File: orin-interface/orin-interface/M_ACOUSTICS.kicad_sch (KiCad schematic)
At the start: 19 parts, among them T6 749022310

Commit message: orin-interface: PoE channels, buses, 3V3 regulator, ERC fixes
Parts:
- C52, C53, C54, C55, C56, C57, C58, C59, C60, C61: footprint (none) -> Capacitor_SMD:C_0603_1608Metric_Pad1.08x0.95mm_HandSolder
- R32, R36, R40, R44, R57, R58, R59, R60: footprint (none) -> Resistor_SMD:R_0603_1608Metric_Pad0.98x0.95mm_HandSolder
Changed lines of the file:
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@@
 			)
 		)
-		(property "Footprint" ""
+		(property "Footprint" "Resistor_SMD:R_0603_1608Metric_Pad0.98x0.95mm_HandSolder"
 			(at 119.38 74.93 0)
 			(hide yes)
@@
 			)
 		)
-		(property "Footprint" ""
+		(property "Footprint" "Capacitor_SMD:C_0603_1608Metric_Pad1.08x0.95mm_HandSolder"
 			(at 83.82 81.28 0)
 			(hide yes)
@@
 			)
 		)
-		(property "Footprint" ""
+		(property "Footprint" "Capacitor_SMD:C_0603_1608Metric_Pad1.08x0.95mm_HandSolder"
 			(at 86.36 88.9 0)
 			(hide yes)
@@
 			)
 		)
-		(property "Footprint" ""
+		(property "Footprint" "Resistor_SMD:R_0603_1608Metric_Pad0.98x0.95mm_HandSolder"
 			(at 88.9 74.93 0)
 			(hide yes)
@@
 			)
 		)
-		(property "Footprint" ""
+		(property "Footprint" "Resistor_SMD:R_0603_1608Metric_Pad0.98x0.95mm_HandSolder"
 			(at 124.46 74.93 0)
 			(hide yes)
@@
 			)
 		)
-		(property "Footprint" ""
+		(property "Footprint" "Resistor_SMD:R_0603_1608Metric_Pad0.98x0.95mm_HandSolder"
 			(at 93.98 74.93 0)
 			(hide yes)
@@
 			)
 		)
-		(property "Footprint" ""
+		(property "Footprint" "Capacitor_SMD:C_0603_1608Metric_Pad1.08x0.95mm_HandSolder"
 			(at 119.38 81.28 0)
 			(hide yes)
@@
 			)
 		)
-		(property "Footprint" ""
+		(property "Footprint" "Resistor_SMD:R_0603_1608Metric_Pad0.98x0.95mm_HandSolder"
 			(at 78.74 74.93 0)
 			(hide yes)
@@
 			)
 		)
-		(property "Footprint" ""
+		(property "Footprint" "Capacitor_SMD:C_0603_1608Metric_Pad1.08x0.95mm_HandSolder"
 			(at 78.74 81.28 0)
 			(hide yes)
@@
 			)
 		)
-		(property "Footprint" ""
+		(property "Footprint" "Resistor_SMD:R_0603_1608Metric_Pad0.98x0.95mm_HandSolder"
 			(at 129.54 74.93 0)
 			(hide yes)
@@
 			)
 		)
-		(property "Footprint" ""
+		(property "Footprint" "Capacitor_SMD:C_0603_1608Metric_Pad1.08x0.95mm_HandSolder"
 			(at 88.9 81.28 0)
 			(hide yes)
@@
 			)
 		)
-		(property "Footprint" ""
+		(property "Footprint" "Capacitor_SMD:C_0603_1608Metric_Pad1.08x0.95mm_HandSolder"
 			(at 93.98 81.28 0)
 			(hide yes)
@@
 			)
 		)
-		(property "Footprint" ""
+		(property "Footprint" "Capacitor_SMD:C_0603_1608Metric_Pad1.08x0.95mm_HandSolder"
 			(at 129.54 81.28 0)
 			(hide yes)
@@
 			)
 		)
-		(property "Footprint" ""
+		(property "Footprint" "Capacitor_SMD:C_0603_1608Metric_Pad1.08x0.95mm_HandSolder"
 			(at 124.46 81.28 0)
 			(hide yes)
@@
 			)
 		)
-		(property "Footprint" ""
+		(property "Footprint" "Resistor_SMD:R_0603_1608Metric_Pad0.98x0.95mm_HandSolder"
 			(at 134.62 74.93 0)
 			(hide yes)
@@
 			)
 		)
-		(property "Footprint" ""
+		(property "Footprint" "Capacitor_SMD:C_0603_1608Metric_Pad1.08x0.95mm_HandSolder"
 			(at 127 88.9 0)
 			(hide yes)
@@
 			)
 		)
-		(property "Footprint" ""
+		(property "Footprint" "Resistor_SMD:R_0603_1608Metric_Pad0.98x0.95mm_HandSolder"
 			(at 83.82 74.93 0)
 			(hide yes)
@@
 			)
 		)
-		(property "Footprint" ""
+		(property "Footprint" "Capacitor_SMD:C_0603_1608Metric_Pad1.08x0.95mm_HandSolder"
 			(at 134.62 81.28 0)
 			(hide yes)

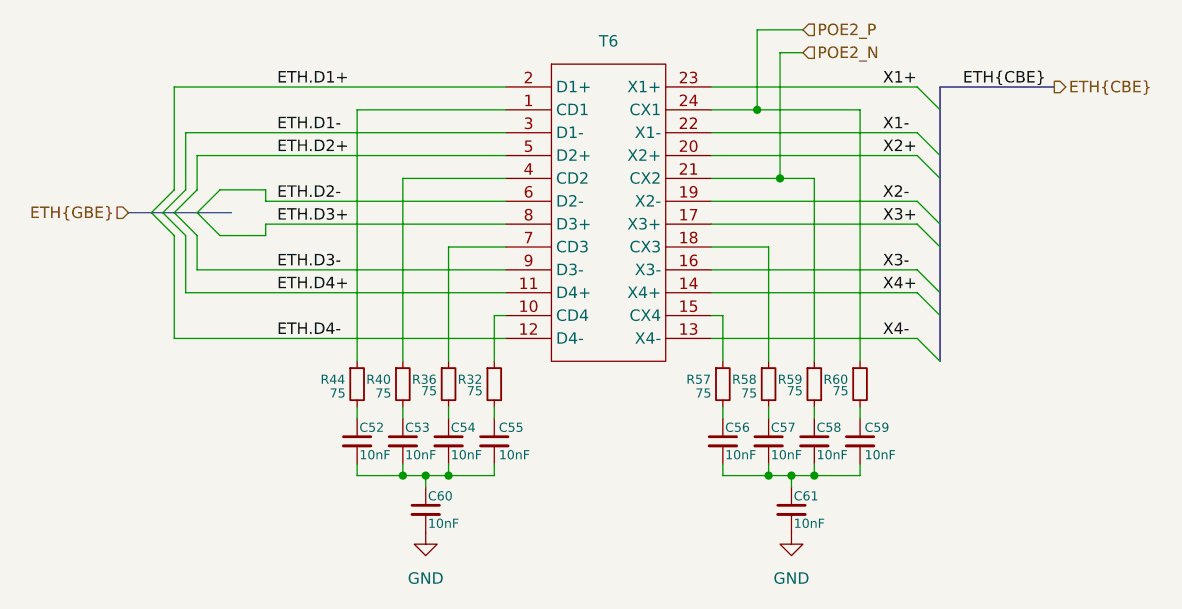
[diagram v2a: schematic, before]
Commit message: orin-interface: add ETH connector sheets and Mate-connectors footprint lib; update orin-bob
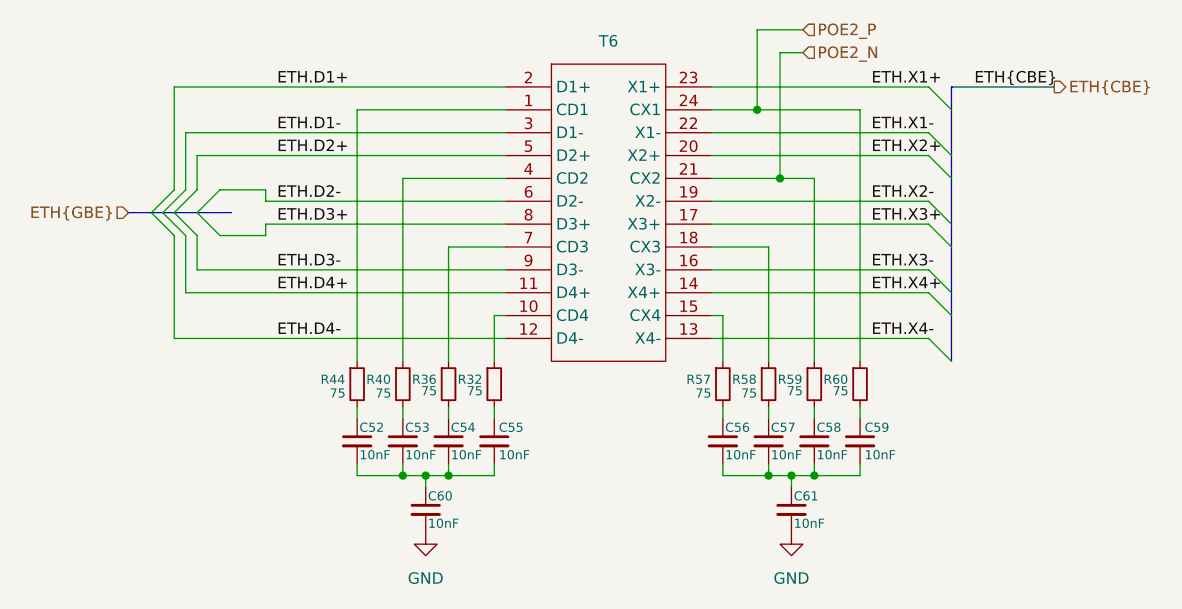
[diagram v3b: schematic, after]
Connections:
- net X1+ renamed ETH.X1+
- net X1- renamed ETH.X1-
- net X2+ renamed ETH.X2+
- net X2- renamed ETH.X2-
- net X3+ renamed ETH.X3+
- net X3- renamed ETH.X3-
- net X4+ renamed ETH.X4+
- net X4- renamed ETH.X4-
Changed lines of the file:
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@@
 	)
 	(bus_entry
-		(at 140.97 69.85)
+		(at 142.24 69.85)
 		(size 2.54 2.54)
 		(stroke
@@
 	)
 	(bus_entry
-		(at 140.97 41.91)
-		(size 2.54 2.54)
-		(stroke
-			(width 0)
-			(type default)
-		)
-	)
-	(bus_entry
-		(at 140.97 62.23)
+		(at 142.24 41.91)
+		(size 2.54 2.54)
+		(stroke
+			(width 0)
+			(type default)
+		)
+	)
+	(bus_entry
+		(at 142.24 62.23)
 		(size 2.54 2.54)
 		(stroke
@@
 	)
 	(bus_entry
-		(at 140.97 54.61)
-		(size 2.54 2.54)
-		(stroke
-			(width 0)
-			(type default)
-		)
-	)
-	(bus_entry
-		(at 140.97 64.77)
+		(at 142.24 54.61)
+		(size 2.54 2.54)
+		(stroke
+			(width 0)
+			(type default)
+		)
+	)
+	(bus_entry
+		(at 142.24 64.77)
 		(size 2.54 2.54)
 		(stroke
@@
 	)
 	(bus_entry
-		(at 140.97 57.15)
+		(at 142.24 57.15)
 		(size 2.54 2.54)
 		(stroke
@@
 	)
 	(bus_entry
-		(at 140.97 46.99)
-		(size 2.54 2.54)
-		(stroke
-			(width 0)
-			(type default)
-		)
-	)
-	(bus_entry
-		(at 140.97 49.53)
+		(at 142.24 46.99)
+		(size 2.54 2.54)
+		(stroke
+			(width 0)
+			(type default)
+		)
+	)
+	(bus_entry
+		(at 142.24 49.53)
 		(size 2.54 2.54)
 		(stroke
@@
 	(wire
 		(pts
-			(xy 118.11 49.53) (xy 140.97 49.53)
+			(xy 118.11 49.53) (xy 142.24 49.53)
 		)
 		(stroke
@@
 	(wire
 		(pts
-			(xy 118.11 41.91) (xy 140.97 41.91)
+			(xy 118.11 41.91) (xy 142.24 41.91)
 		)
 		(stroke
@@
 	(wire
 		(pts
-			(xy 118.11 62.23) (xy 140.97 62.23)
+			(xy 118.11 62.23) (xy 142.24 62.23)
 		)
 		(stroke
@@
 	(wire
 		(pts
-			(xy 118.11 46.99) (xy 140.97 46.99)
+			(xy 118.11 46.99) (xy 142.24 46.99)
 		)
 		(stroke
@@
 	(wire
 		(pts
-			(xy 118.11 57.15) (xy 140.97 57.15)
-		)
-		(stroke
-			(width 0)
-			(type default)
-		)
-	)
-	(wire
-		(pts
-			(xy 118.11 69.85) (xy 140.97 69.85)
-		)
-		(stroke
-			(width 0)
-			(type default)
-		)
-	)
-	(wire
-		(pts
-			(xy 118.11 64.77) (xy 140.97 64.77)
+			(xy 118.11 57.15) (xy 142.24 57.15)
+		)
+		(stroke
+			(width 0)
+			(type default)
+		)
+	)
+	(wire
+		(pts
+			(xy 118.11 69.85) (xy 142.24 69.85)
+		)
+		(stroke
+			(width 0)
+			(type default)
+		)
+	)
+	(wire
+		(pts
+			(xy 118.11 64.77) (xy 142.24 64.77)
 		)
 		(stroke
@@
 	(bus
 		(pts
-			(xy 143.51 41.91) (xy 156.21 41.91)
-		)
-		(stroke
-			(width 0)
-			(type default)
-		)
-	)
-	(wire
-		(pts
-			(xy 118.11 54.61) (xy 140.97 54.61)
+			(xy 144.78 41.91) (xy 156.21 41.91)
+		)
+		(stroke
+			(width 0)
+			(type default)
+		)
+	)
+	(wire
+		(pts
+			(xy 118.11 54.61) (xy 142.24 54.61)
 		)
 		(stroke
@@
 	(bus
 		(pts
-			(xy 143.51 72.39) (xy 143.51 41.91)
+			(xy 144.78 72.39) (xy 144.78 41.91)
 		)
 		(stroke
@@
 		)
 	)
-	(label "X1+"
-		(at 137.16 41.91 0)
+	(label "ETH.X1+"
+		(at 135.89 41.91 0)
 		(effects
 			(font
@@
 		)
 	)
-	(label "X2-"
-		(at 137.16 54.61 0)
+	(label "ETH.X2-"
+		(at 135.89 54.61 0)
 		(effects
 			(font
@@
 		)
 	)
-	(label "X4+"
-		(at 137.16 64.77 0)
-		(effects
-			(font
-				(size 1.27 1.27)
-			)
-			(justify left bottom)
-		)
-	)
-	(label "X2+"
-		(at 137.16 49.53 0)
-		(effects
-			(font
-				(size 1.27 1.27)
-			)
-			(justify left bottom)
-		)
-	)
-	(label "X3-"
-		(at 137.16 62.23 0)
-		(effects
-			(font
-				(size 1.27 1.27)
-			)
-			(justify left bottom)
-		)
-	)
-	(label "X3+"
-		(at 137.16 57.15 0)
-		(effects
-			(font
-				(size 1.27 1.27)
-			)
-			(justify left bottom)
-		)
-	)
-	(label "X4-"
-		(at 137.16 69.85 0)
+	(label "ETH.X4+"
+		(at 135.89 64.77 0)
+		(effects
+			(font
+				(size 1.27 1.27)
+			)
+			(justify left bottom)
+		)
+	)
+	(label "ETH.X2+"
+		(at 135.89 49.53 0)
+		(effects
+			(font
+				(size 1.27 1.27)
+			)
+			(justify left bottom)
+		)
+	)
+	(label "ETH.X3-"
+		(at 135.89 62.23 0)
+		(effects
+			(font
+				(size 1.27 1.27)
+			)
+			(justify left bottom)
+		)
+	)
+	(label "ETH.X3+"
+		(at 135.89 57.15 0)
+		(effects
+			(font
+				(size 1.27 1.27)
+			)
+			(justify left bottom)
+		)
+	)
+	(label "ETH.X4-"
+		(at 135.89 69.85 0)
 		(effects
 			(font
@@
 	)
 	(label "ETH{CBE}"
-		(at 146.05 41.91 0)
+		(at 147.32 41.91 0)
 		(effects
 			(font
@@
 		)
 	)
-	(label "X1-"
-		(at 137.16 46.99 0)
-		(effects
-			(font
+	(label "ETH.X1-"
+		(at 135.89 46.99 0)
+		(effects
+			(font

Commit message: finished v2 schematic
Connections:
- net POE2_N renamed POE4_N
- net POE2_P renamed POE4_P
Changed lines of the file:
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@@
 		)
 	)
-	(hierarchical_label "POE2_N"
+	(hierarchical_label "POE4_N"
 		(shape input)
 		(at 128.27 38.1 0)
@@
 		)
 	)
-	(hierarchical_label "POE2_P"
+	(hierarchical_label "POE4_P"
 		(shape input)
 		(at 128.27 35.56 0)
